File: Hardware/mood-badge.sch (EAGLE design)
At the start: 90 parts

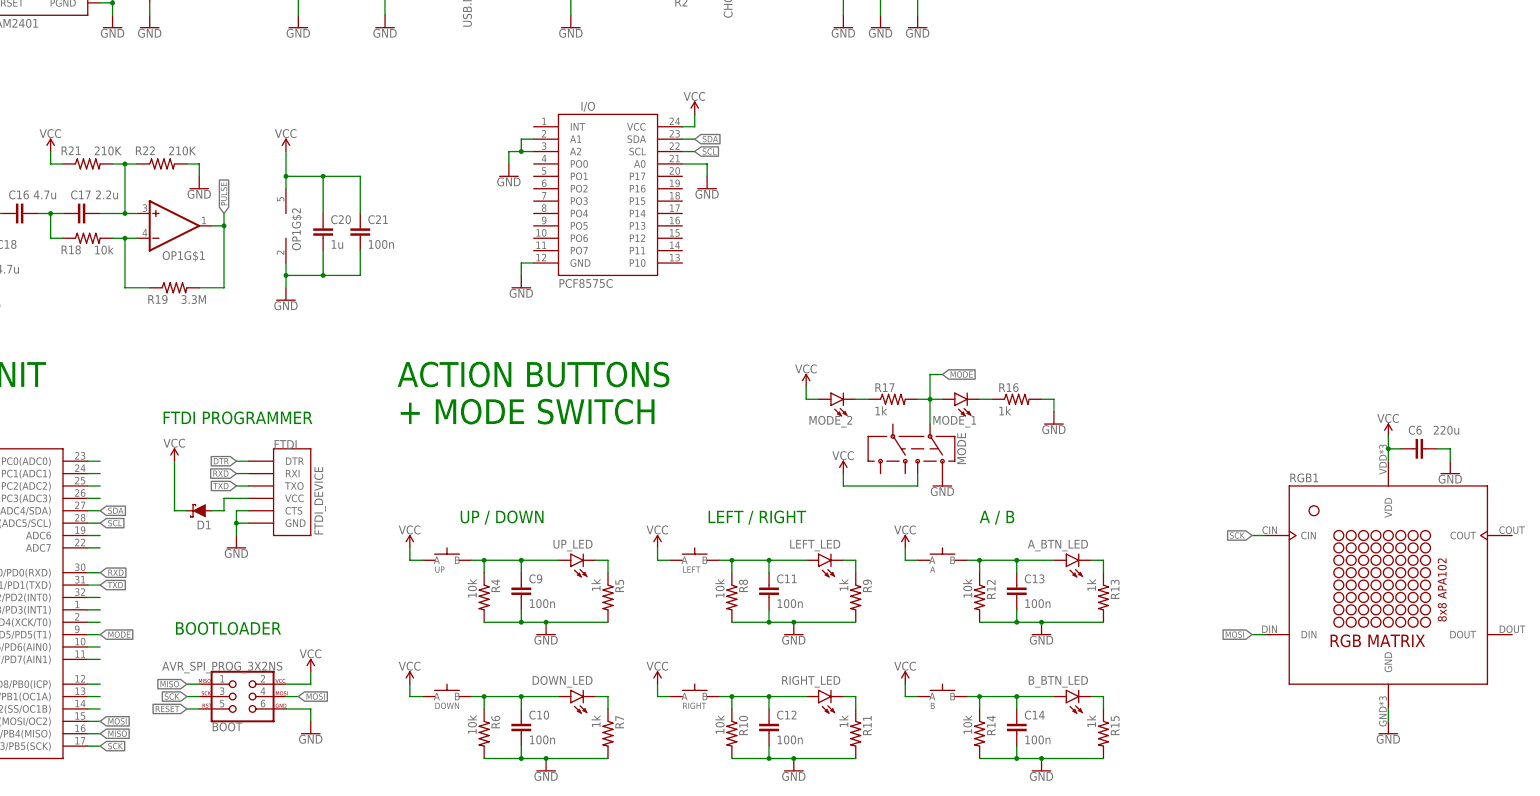
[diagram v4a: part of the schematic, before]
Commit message: Adjustments to PCB trace widths and connections to buttons added
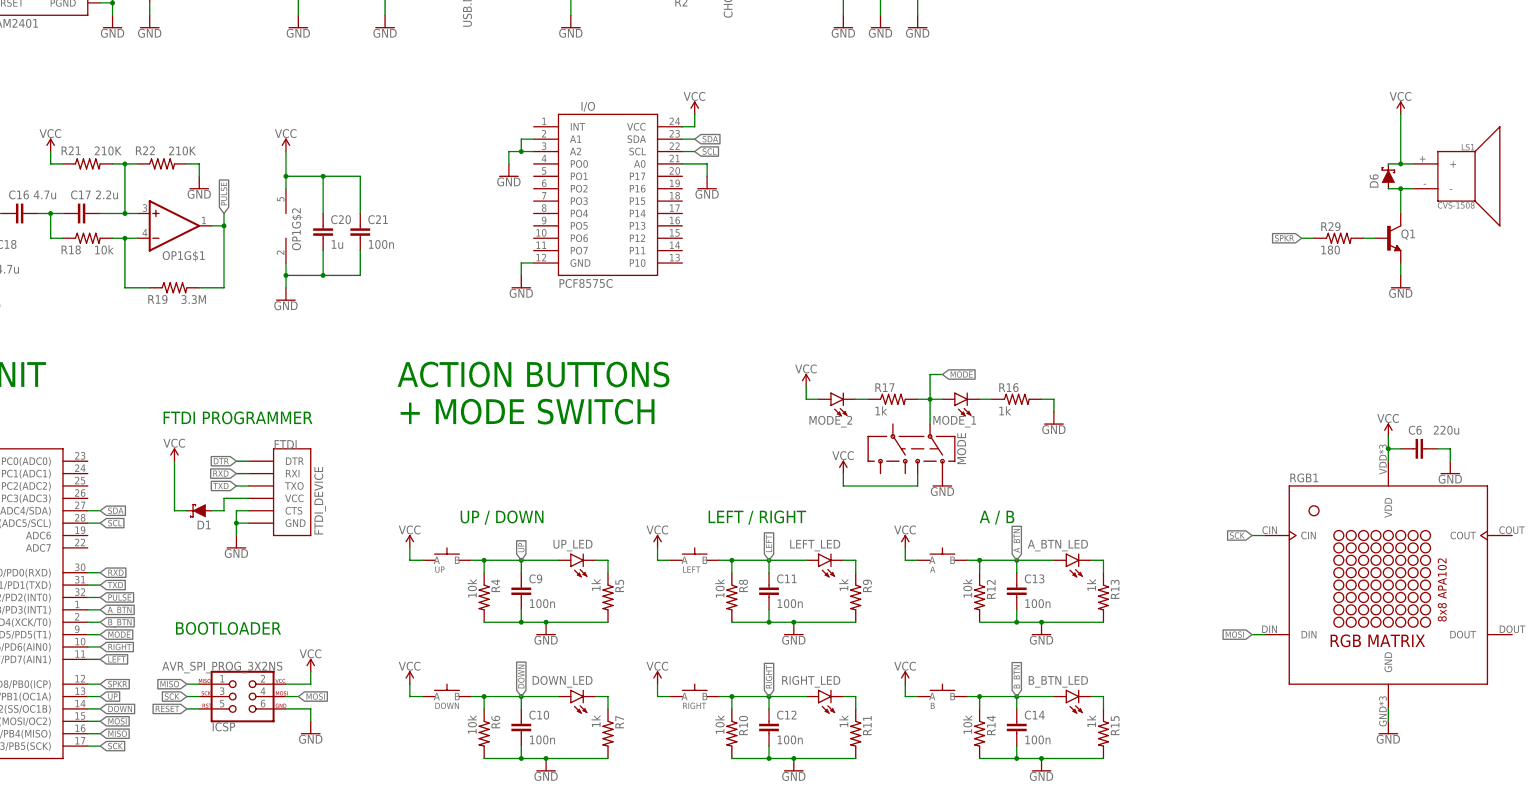
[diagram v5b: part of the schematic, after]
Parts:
- added D6: (no value), LinnesLab-DiscreteSemi:SCHOTTKY-USC
- added LS1: CVS-1508, SparkFun-Electromechanical:SPEAKERCVS-1508
- added Q1: (no value), LinnesLab-DiscreteSemi:NPN-GENERIC
- added R29: 180, LinnesLab-Passives:RESISTOR0603
- renumbered BOOT to ICSP
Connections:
- removed net ACTION: ARDUINO.ADC6
- removed net LD1: ARDUINO.D4/PD4(XCK/T0)
- removed net LD12: ARDUINO.D10/PB2(SS/OC1B)
- removed net LD13: ARDUINO.D9/PB1(OC1A)
- removed net LD14: ARDUINO.D8/PB0(ICP)
- removed net LD15: ARDUINO.D7/PD7(AIN1)
- removed net LD16: ARDUINO.D6/PD6(AIN0)
- removed net LD2: ARDUINO.D3/PD3(INT1)
- removed net LD3: ARDUINO.D2/PD2(INT0)
- removed net LD6: ARDUINO.PC3(ADC3)
- removed net LD7: ARDUINO.PC2(ADC2)
- removed net LD8: ARDUINO.PC1(ADC1)
- removed net N$10: C10.1, DOWN.B, DOWN_LED.A, R6.1
- removed net N$12: C11.1, LEFT.B, LEFT_LED.A, R8.1
- removed net N$14: C12.1, R10.1, RIGHT.B, RIGHT_LED.A
- removed net N$16: A.B, A_BTN_LED.A, C13.1, R12.1
- removed net N$18: B.B, B_BTN_LED.A, C14.1, R14.1
- removed net N$8: C9.1, R4.1, UP.B, UP_LED.A
- new net A_BTN: A.B, ARDUINO.D3/PD3(INT1), A_BTN_LED.A, C13.1, R12.1
- new net B_BTN: ARDUINO.D4/PD4(XCK/T0), B.B, B_BTN_LED.A, C14.1, R14.1
- new net DOWN: ARDUINO.D10/PB2(SS/OC1B), C10.1, DOWN.B, DOWN_LED.A, R6.1
- new net N$31: Q1.B, R29.2
- new net N$5: D6.A, LS1.-, Q1.C
- new net SPKR: ARDUINO.D8/PB0(ICP), R29.1
- new net UP: ARDUINO.D9/PB1(OC1A), C9.1, R4.1, UP.B, UP_LED.A
- net GND: now also Q1.E
- net LEFT: now also ARDUINO.D7/PD7(AIN1), C11.1, LEFT.B, LEFT_LED.A, R8.1; no longer ARDUINO.PC0(ADC0)
- net PULSE: now also ARDUINO.D2/PD2(INT0)
- net RIGHT: now also ARDUINO.D6/PD6(AIN0), C12.1, R10.1, RIGHT.B, RIGHT_LED.A; no longer ARDUINO.ADC7
- net VCC: now also D6.C, LS1.+

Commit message: PCB Routed
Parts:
- removed I/O: PCF8575C, SparkFun-Retired:PCF8575C
- renumbered CHG_LED to CHG, PWR_LED to PWR
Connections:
- removed net N$22: MODE_1.C, R16.1
- new net N$8: MODE_1.A, R16.2
- net A_BTN: now also ARDUINO.D6/PD6(AIN0); no longer ARDUINO.D3/PD3(INT1)
- net B_BTN: now also ARDUINO.D5/PD5(T1); no longer ARDUINO.D4/PD4(XCK/T0)
- net DOWN: now also ARDUINO.D8/PB0(ICP); no longer ARDUINO.D10/PB2(SS/OC1B)
- net GND: now also MODE_1.C; no longer I/O.A0, I/O.A1, I/O.A2, I/O.GND, R16.2
- net LEFT: now also ARDUINO.D9/PB1(OC1A); no longer ARDUINO.D7/PD7(AIN1)
- net MODE: now also ARDUINO.D4/PD4(XCK/T0), R16.1; no longer ARDUINO.D5/PD5(T1), MODE_1.A
- net RIGHT: now also ARDUINO.D7/PD7(AIN1); no longer ARDUINO.D6/PD6(AIN0)
- net SCL: no longer I/O.SCL
- net SDA: no longer I/O.SDA
- net SPKR: now also ARDUINO.D3/PD3(INT1); no longer ARDUINO.D8/PB0(ICP)
- net UP: now also ARDUINO.D10/PB2(SS/OC1B); no longer ARDUINO.D9/PB1(OC1A)
- net VCC: no longer I/O.VCC
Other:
- moved on the sheet: MODE_1, R16

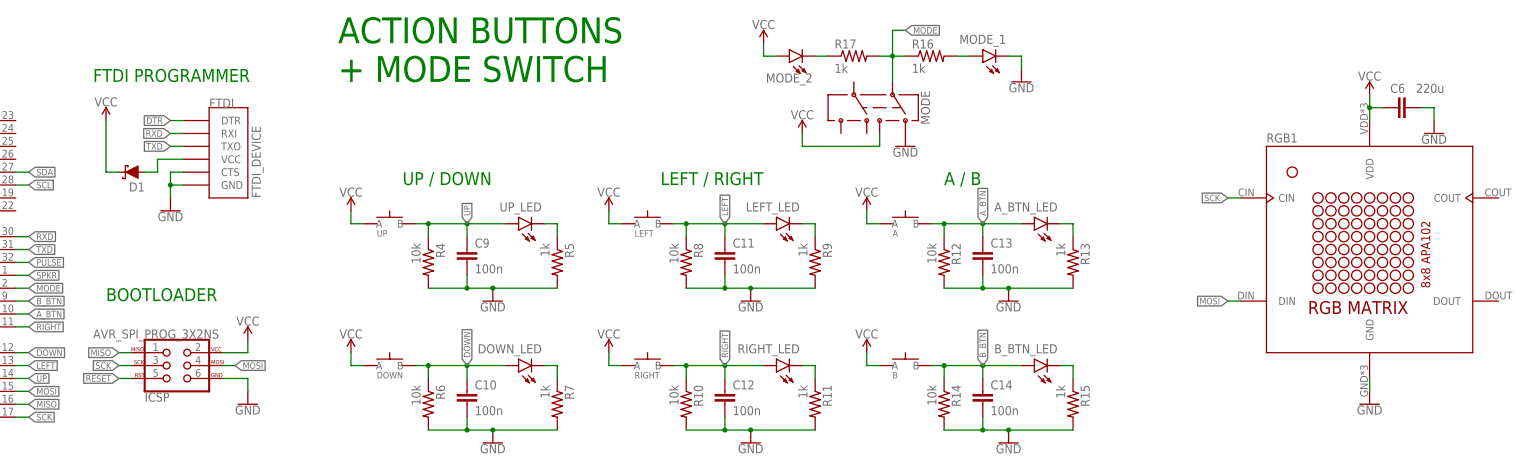
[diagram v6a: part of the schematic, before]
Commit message: Swap out matrix for different part with better connector layout
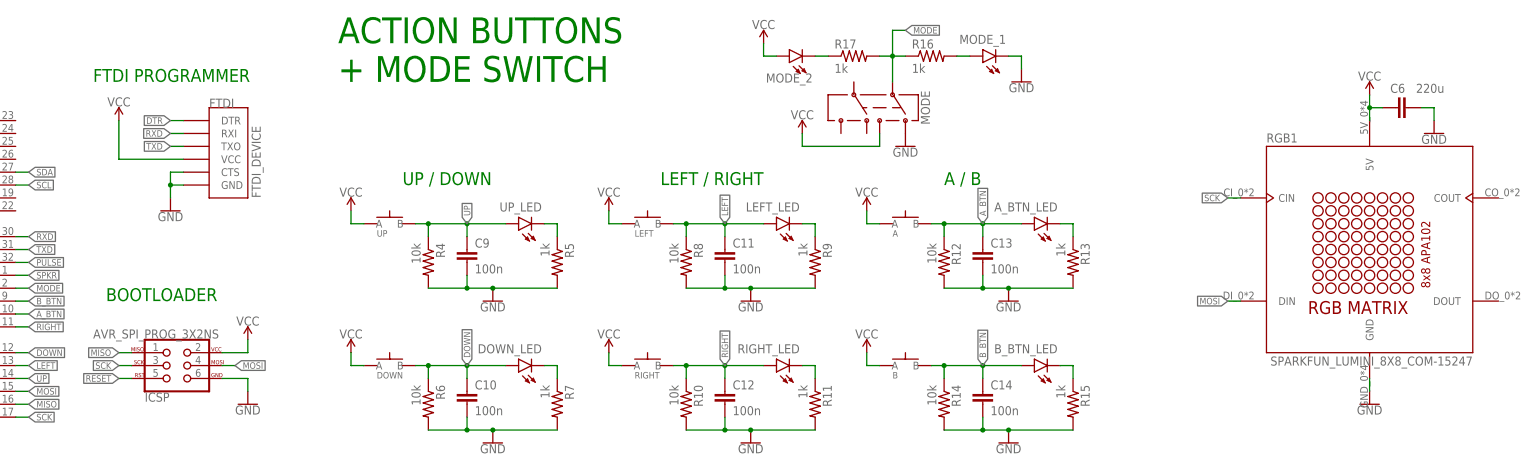
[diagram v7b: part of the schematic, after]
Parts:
- removed D1: (no value), LinnesLab-DiscreteSemi:SCHOTTKY-USC
- LED1: device LinnesLab-LED:LED0603 -> LinnesLab-LED:LEDZ-BEND
- RGB1: value (none) -> SPARKFUN_LUMINI_8X8_COM-15247; device mood-badge-components:ADA_DOTSTAR_8X8_34448X8_DOTSTAR_3444_HOLES -> mood-badge-components:SPARKFUN_LUMINI_8X8_COM-15247
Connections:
- removed net N$6: D1.A, FTDI.VCC
- net VCC: now also FTDI.VCC, RGB1.5V; no longer D1.C, RGB1.VDD

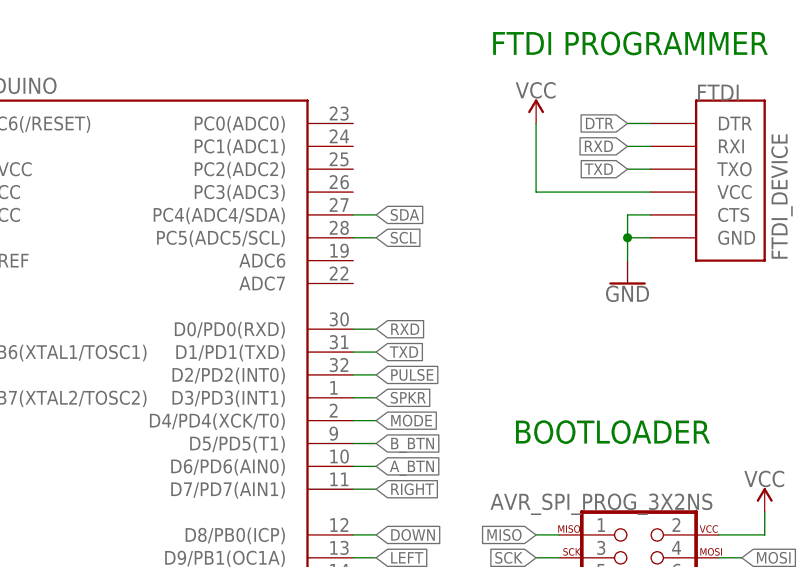
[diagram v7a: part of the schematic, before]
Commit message: Minor fixes and routing changes
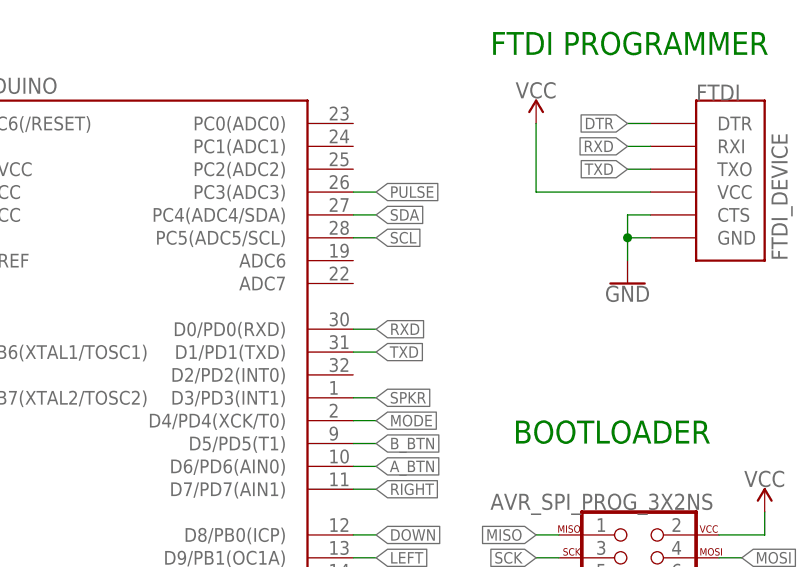
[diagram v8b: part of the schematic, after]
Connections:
- net PULSE: now also ARDUINO.PC3(ADC3); no longer ARDUINO.D2/PD2(INT0)
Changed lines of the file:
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@@
 <grid distance="0.1" unitdist="inch" unit="inch" style="lines" multiple="1" display="no" altdistance="0.01" altunitdist="inch" altunit="inch"/>
 <layers>
-<layer number="1" name="Top" color="4" fill="1" visible="yes" active="no"/>
-<layer number="2" name="Route2" color="1" fill="3" visible="yes" active="no"/>
-<layer number="3" name="Route3" color="4" fill="3" visible="yes" active="no"/>
-<layer number="4" name="Route4" color="1" fill="4" visible="yes" active="no"/>
-<layer number="5" name="Route5" color="4" fill="4" visible="yes" active="no"/>
-<layer number="6" name="Route6" color="1" fill="8" visible="yes" active="no"/>
-<layer number="7" name="Route7" color="4" fill="8" visible="yes" active="no"/>
-<layer number="8" name="Route8" color="1" fill="2" visible="yes" active="no"/>
-<layer number="9" name="Route9" color="4" fill="2" visible="yes" active="no"/>
-<layer number="10" name="Route10" color="1" fill="7" visible="yes" active="no"/>
-<layer number="11" name="Route11" color="4" fill="7" visible="yes" active="no"/>
-<layer number="12" name="Route12" color="1" fill="5" visible="yes" active="no"/>
-<layer number="13" name="Route13" color="4" fill="5" visible="yes" active="no"/>
-<layer number="14" name="Route14" color="1" fill="6" visible="yes" active="no"/>
-<layer number="15" name="Route15" color="4" fill="6" visible="yes" active="no"/>
-<layer number="16" name="Bottom" color="1" fill="1" visible="yes" active="no"/>
-<layer number="17" name="Pads" color="2" fill="1" visible="yes" active="no"/>
-<layer number="18" name="Vias" color="2" fill="1" visible="yes" active="no"/>
-<layer number="19" name="Unrouted" color="6" fill="1" visible="yes" active="no"/>
-<layer number="20" name="Dimension" color="24" fill="1" visible="yes" active="no"/>
-<layer number="21" name="tPlace" color="7" fill="1" visible="yes" active="no"/>
-<layer number="22" name="bPlace" color="7" fill="1" visible="yes" active="no"/>
-<layer number="23" name="tOrigins" color="15" fill="1" visible="yes" active="no"/>
-<layer number="24" name="bOrigins" color="15" fill="1" visible="yes" active="no"/>
-<layer number="25" name="tNames" color="7" fill="1" visible="yes" active="no"/>
-<layer number="26" name="bNames" color="7" fill="1" visible="yes" active="no"/>
-<layer number="27" name="tValues" color="7" fill="1" visible="yes" active="no"/>
-<layer number="28" name="bValues" color="7" fill="1" visible="yes" active="no"/>
+<layer number="1" name="Top" color="4" fill="1" visible="no" active="no"/>
+<layer number="2" name="Route2" color="1" fill="3" visible="no" active="no"/>
+<layer number="3" name="Route3" color="4" fill="3" visible="no" active="no"/>
+<layer number="4" name="Route4" color="1" fill="4" visible="no" active="no"/>
+<layer number="5" name="Route5" color="4" fill="4" visible="no" active="no"/>
+<layer number="6" name="Route6" color="1" fill="8" visible="no" active="no"/>
+<layer number="7" name="Route7" color="4" fill="8" visible="no" active="no"/>
+<layer number="8" name="Route8" color="1" fill="2" visible="no" active="no"/>
+<layer number="9" name="Route9" color="4" fill="2" visible="no" active="no"/>
+<layer number="10" name="Route10" color="1" fill="7" visible="no" active="no"/>
+<layer number="11" name="Route11" color="4" fill="7" visible="no" active="no"/>
+<layer number="12" name="Route12" color="1" fill="5" visible="no" active="no"/>
+<layer number="13" name="Route13" color="4" fill="5" visible="no" active="no"/>
+<layer number="14" name="Route14" color="1" fill="6" visible="no" active="no"/>
+<layer number="15" name="Route15" color="4" fill="6" visible="no" active="no"/>
+<layer number="16" name="Bottom" color="1" fill="1" visible="no" active="no"/>
+<layer number="17" name="Pads" color="2" fill="1" visible="no" active="no"/>
+<layer number="18" name="Vias" color="2" fill="1" visible="no" active="no"/>
+<layer number="19" name="Unrouted" color="6" fill="1" visible="no" active="no"/>
+<layer number="20" name="Dimension" color="24" fill="1" visible="no" active="no"/>
+<layer number="21" name="tPlace" color="7" fill="1" visible="no" active="no"/>
+<layer number="22" name="bPlace" color="7" fill="1" visible="no" active="no"/>
+<layer number="23" name="tOrigins" color="15" fill="1" visible="no" active="no"/>
+<layer number="24" name="bOrigins" color="15" fill="1" visible="no" active="no"/>
+<layer number="25" name="tNames" color="7" fill="1" visible="no" active="no"/>
+<layer number="26" name="bNames" color="7" fill="1" visible="no" active="no"/>
+<layer number="27" name="tValues" color="7" fill="1" visible="no" active="no"/>
+<layer number="28" name="bValues" color="7" fill="1" visible="no" active="no"/>
 <layer number="29" name="tStop" color="7" fill="3" visible="no" active="no"/>
 <layer number="30" name="bStop" color="7" fill="6" visible="no" active="no"/>
@@
 <layer number="35" name="tGlue" color="7" fill="4" visible="no" active="no"/>
 <layer number="36" name="bGlue" color="7" fill="5" visible="no" active="no"/>
-<layer number="37" name="tTest" color="7" fill="1" visible="yes" active="no"/>
-<layer number="38" name="bTest" color="7" fill="1" visible="yes" active="no"/>
+<layer number="37" name="tTest" color="7" fill="1" visible="no" active="no"/>
+<layer number="38" name="bTest" color="7" fill="1" visible="no" active="no"/>
 <layer number="39" name="tKeepout" color="4" fill="11" visible="no" active="no"/>
 <layer number="40" name="bKeepout" color="1" fill="11" visible="no" active="no"/>
@@
 <layer number="44" name="Drills" color="7" fill="1" visible="no" active="no"/>
 <layer number="45" name="Holes" color="7" fill="1" visible="no" active="no"/>
-<layer number="46" name="Milling" color="3" fill="1" visible="yes" active="no"/>
-<layer number="47" name="Measures" color="7" fill="1" visible="yes" active="no"/>
-<layer number="48" name="Document" color="7" fill="1" visible="yes" active="no"/>
-<layer number="49" name="Reference" color="7" fill="1" visible="yes" active="no"/>
-<layer number="50" name="dxf" color="7" fill="1" visible="yes" active="no"/>
-<layer number="51" name="tDocu" color="7" fill="1" visible="yes" active="no"/>
-<layer number="52" name="bDocu" color="7" fill="1" visible="yes" active="no"/>
-<layer number="53" name="tGND_GNDA" color="7" fill="9" visible="yes" active="no"/>
-<layer number="54" name="bGND_GNDA" color="1" fill="9" visible="yes" active="no"/>
-<layer number="56" name="wert" color="7" fill="1" visible="yes" active="no"/>
-<layer number="57" name="tCAD" color="7" fill="1" visible="yes" active="no"/>
-<layer number="59" name="tCarbon" color="7" fill="1" visible="yes" active="no"/>
-<layer number="60" name="bCarbon" color="7" fill="1" visible="yes" active="no"/>
+<layer number="46" name="Milling" color="3" fill="1" visible="no" active="no"/>
+<layer number="47" name="Measures" color="7" fill="1" visible="no" active="no"/>
+<layer number="48" name="Document" color="7" fill="1" visible="no" active="no"/>
+<layer number="49" name="Reference" color="7" fill="1" visible="no" active="no"/>
+<layer number="50" name="dxf" color="7" fill="1" visible="no" active="no"/>
+<layer number="51" name="tDocu" color="7" fill="1" visible="no" active="no"/>
+<layer number="52" name="bDocu" color="7" fill="1" visible="no" active="no"/>
+<layer number="53" name="tGND_GNDA" color="7" fill="9" visible="no" active="no"/>
+<layer number="54" name="bGND_GNDA" color="1" fill="9" visible="no" active="no"/>
+<layer number="56" name="wert" color="7" fill="1" visible="no" active="no"/>
+<layer number="57" name="tCAD" color="7" fill="1" visible="no" active="no"/>
+<layer number="59" name="tCarbon" color="7" fill="1" visible="no" active="no"/>
+<layer number="60" name="bCarbon" color="7" fill="1" visible="no" active="no"/>
 <layer number="88" name="SimResults" color="9" fill="1" visible="yes" active="yes"/>
 <layer number="89" name="SimProbes" color="9" fill="1" visible="yes" active="yes"/>
@@
 </segment>
 <segment>
-<pinref part="ARDUINO" gate="U$1" pin="D2/PD2(INT0)"/>
-<wire x1="93.98" y1="43.18" x2="96.52" y2="43.18" width="0.1524" layer="91"/>
-<label x="96.52" y="43.18" size="1.27" layer="95" xref="yes"/>
-</segment>
-</net>
+<pinref part="ARDUINO" gate="U$1" pin="PC3(ADC3)"/>
+<wire x1="93.98" y1="63.5" x2="96.52" y2="63.5" width="0.1524" layer="91"/>
+<label x="96.52" y="63.5" size="1.27" layer="95" xref="yes"/>
+</segment>
+</net>
